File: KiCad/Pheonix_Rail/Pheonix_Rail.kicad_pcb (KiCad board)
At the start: 2 copper layers, 127 x 19.7 mm, 15 parts, among them J1 1729128, J10 1729128, J11 1729128, J12 1729128, J13 1729128, J2 1729128, J3 1729128, J4 1729128, J5 1729128, J6 1729128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

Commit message: commit
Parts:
- moved H2 170.9 mm to (267.2, 74.0)
- moved J1 90.0 mm to (144.3, 69.4)
- moved H1 62.9 mm to (145.8, 74.0)
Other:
- board size 127 x 19.7 mm -> 127 x 26 mm
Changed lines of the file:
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@@
 	)
 	(setup
+		(stackup
+			(layer "F.SilkS"
+				(type "Top Silk Screen")
+			)
+			(layer "F.Paste"
+				(type "Top Solder Paste")
+			)
+			(layer "F.Mask"
+				(type "Top Solder Mask")
+				(thickness 0.01)
+			)
+			(layer "F.Cu"
+				(type "copper")
+				(thickness 0.035)
+			)
+			(layer "dielectric 1"
+				(type "core")
+				(thickness 1.51)
+				(material "FR4")
+				(epsilon_r 4.5)
+				(loss_tangent 0.02)
+			)
+			(layer "B.Cu"
+				(type "copper")
+				(thickness 0.035)
+			)
+			(layer "B.Mask"
+				(type "Bottom Solder Mask")
+				(thickness 0.01)
+			)
+			(layer "B.Paste"
+				(type "Bottom Solder Paste")
+			)
+			(layer "B.SilkS"
+				(type "Bottom Silk Screen")
+			)
+			(copper_finish "None")
+			(dielectric_constraints no)
+		)
 		(pad_to_mask_clearance 0)
 		(allow_soldermask_bridges_in_footprints no)
@@
 	(footprint "MountingHole:MountingHole_2.5mm"
 		(layer "F.Cu")
-		(at 100.37 30.5)
+		(at 145.75 74)
 		(descr "Mounting Hole 2.5mm, no annular, generated by kicad-footprint-generator mountinghole.py")
 		(tags "mountinghole")
@@
 	(footprint "1729128:PHOENIX_1729128"
 		(layer "F.Cu")
-		(at 60.695 36.15)
+		(at 144.275 69.4)
 		(property "Reference" "J1"
 			(at 3.175 -9.135 0)
@@
 	(footprint "MountingHole:MountingHole_2.5mm"
 		(layer "F.Cu")
-		(at 100.37 37.05)
+		(at 267.25 74)
 		(descr "Mounting Hole 2.5mm, no annular, generated by kicad-footprint-generator mountinghole.py")
 		(tags "mountinghole")
@@
 	)
 	(gr_rect
-		(start 122.32 74.58)
-		(end 249.36 94.27)
+		(start 143 61)
+		(end 270 87)
 		(stroke
 			(width 0.05)

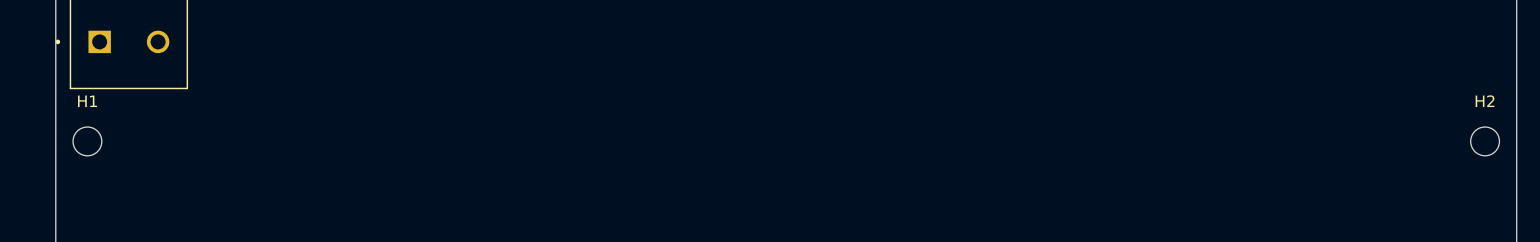
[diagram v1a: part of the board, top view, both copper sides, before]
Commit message: changed mounting holes
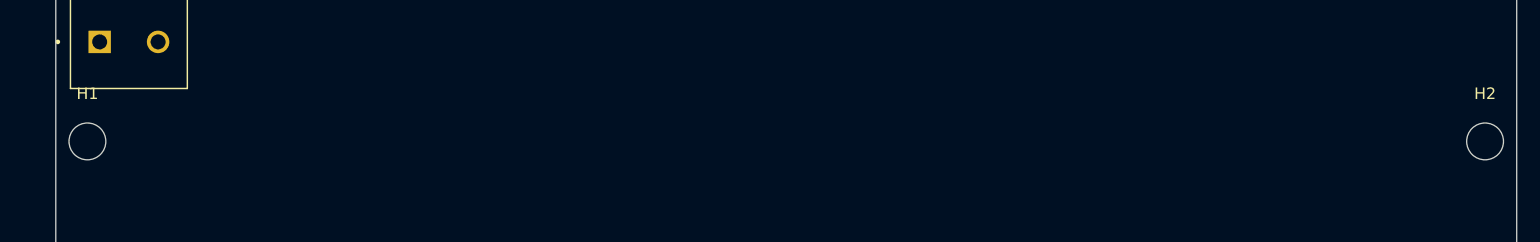
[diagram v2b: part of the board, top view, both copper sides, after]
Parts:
- H1, H2: footprint MountingHole:MountingHole_2.5mm -> MountingHole:MountingHole_3.2mm_M3
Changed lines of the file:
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@@
 		(embedded_fonts no)
 	)
-	(footprint "MountingHole:MountingHole_2.5mm"
+	(footprint "MountingHole:MountingHole_3.2mm_M3"
 		(layer "F.Cu")
 		(at 145.75 74)
-		(descr "Mounting Hole 2.5mm, no annular, generated by kicad-footprint-generator mountinghole.py")
-		(tags "mountinghole")
+		(descr "Mounting Hole 3.2mm, M3, no annular, generated by kicad-footprint-generator mountinghole.py")
+		(tags "mountinghole M3")
 		(property "Reference" "H1"
-			(at 0 -3.45 0)
+			(at 0 -4.15 0)
 			(layer "F.SilkS")
 			(effects
@@
 		)
 		(property "Value" "MountingHole"
-			(at 0 3.45 0)
+			(at 0 4.15 0)
 			(layer "F.Fab")
 			(effects
@@
 		(fp_circle
 			(center 0 0)
-			(end 2.5 0)
+			(end 3.2 0)
 			(stroke
 				(width 0.15)
@@
 		(fp_circle
 			(center 0 0)
-			(end 2.75 0)
+			(end 3.45 0)
 			(stroke
 				(width 0.05)
@@
 		(pad "" np_thru_hole circle
 			(at 0 0)
-			(size 2.5 2.5)
-			(drill 2.5)
+			(size 3.2 3.2)
+			(drill 3.2)
 			(layers "*.Cu" "*.Mask")
 		)
@@
 		(embedded_fonts no)
 	)
-	(footprint "MountingHole:MountingHole_2.5mm"
+	(footprint "MountingHole:MountingHole_3.2mm_M3"
 		(layer "F.Cu")
 		(at 267.25 74)
-		(descr "Mounting Hole 2.5mm, no annular, generated by kicad-footprint-generator mountinghole.py")
-		(tags "mountinghole")
+		(descr "Mounting Hole 3.2mm, M3, no annular, generated by kicad-footprint-generator mountinghole.py")
+		(tags "mountinghole M3")
 		(property "Reference" "H2"
-			(at 0 -3.45 0)
+			(at 0 -4.15 0)
 			(layer "F.SilkS")
 			(effects
@@
 		)
 		(property "Value" "MountingHole"
-			(at 0 3.45 0)
+			(at 0 4.15 0)
 			(layer "F.Fab")
 			(effects
@@
 		(fp_circle
 			(center 0 0)
-			(end 2.5 0)
+			(end 3.2 0)
 			(stroke
 				(width 0.15)
@@
 		(fp_circle
 			(center 0 0)
-			(end 2.75 0)
+			(end 3.45 0)
 			(stroke
 				(width 0.05)
@@
 		(pad "" np_thru_hole circle
 			(at 0 0)
-			(size 2.5 2.5)
-			(drill 2.5)
+			(size 3.2 3.2)
+			(drill 3.2)
 			(layers "*.Cu" "*.Mask")
 		)

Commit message: layout for phoenix board
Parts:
- moved J7 184.1 mm to (255.9, 70.0)
- moved J6 168.0 mm to (237.9, 70.0)
- moved J13 163.5 mm to (246.9, 85.0)
- moved J5 159.4 mm to (220.0, 70.0)
- moved J12 148.1 mm to (229.0, 85.0)
- moved J4 141.4 mm to (202.0, 70.0)
- moved J11 134.1 mm to (211.0, 85.0)
- moved J3 124.1 mm to (184.0, 70.0)
- moved J10 120.0 mm to (193.0, 85.0)
- moved J2 108.0 mm to (166.0, 70.0)
- moved J9 103.5 mm to (175.0, 85.0)
- moved J8 88.6 mm to (157.0, 85.0)
- moved J1 3.77 mm to (148.0, 70.0)
- moved H1 0.70 mm to (146.4, 74.0), turned to 180 degrees
- moved H2 0.70 mm to (266.6, 74.0), turned to 180 degrees
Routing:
- added copper zone on F.Cu, net +24V
- added copper zone on B.Cu, net GND
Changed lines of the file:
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@@
 	(footprint "1729128:PHOENIX_1729128"
 		(layer "F.Cu")
-		(at 73.43 36.15)
+		(at 237.9475 69.975)
 		(property "Reference" "J6"
-			(at 3.175 -9.135 0)
+			(at 4.5675 1.025 0)
 			(layer "F.SilkS")
 			(effects
@@
 	(footprint "1729128:PHOENIX_1729128"
 		(layer "F.Cu")
-		(at 73.43 45.85)
+		(at 255.9475 69.975)
 		(property "Reference" "J7"
-			(at 3.175 -9.135 0)
+			(at 4.5675 1.025 0)
 			(layer "F.SilkS")
 			(effects
@@
 	(footprint "1729128:PHOENIX_1729128"
 		(layer "F.Cu")
-		(at 73.43 55.55)
+		(at 157 85)
 		(property "Reference" "J8"
 			(at 3.175 -9.135 0)
@@
 	(footprint "1729128:PHOENIX_1729128"
 		(layer "F.Cu")
-		(at 86.165 36.15)
+		(at 211 85)
 		(property "Reference" "J11"
 			(at 3.175 -9.135 0)
@@
 	(footprint "1729128:PHOENIX_1729128"
 		(layer "F.Cu")
-		(at 60.695 55.55)
+		(at 184 70)
 		(property "Reference" "J3"
-			(at 3.175 -9.135 0)
+			(at 4.5675 1 0)
 			(layer "F.SilkS")
 			(effects
@@
 	(footprint "1729128:PHOENIX_1729128"
 		(layer "F.Cu")
-		(at 86.165 55.55)
+		(at 246.9475 84.975)
 		(property "Reference" "J13"
 			(at 3.175 -9.135 0)
@@
 	(footprint "1729128:PHOENIX_1729128"
 		(layer "F.Cu")
-		(at 86.165 45.85)
+		(at 229 85)
 		(property "Reference" "J12"
 			(at 3.175 -9.135 0)
@@
 	(footprint "MountingHole:MountingHole_3.2mm_M3"
 		(layer "F.Cu")
-		(at 145.75 74)
+		(at 146.45 74 180)
 		(descr "Mounting Hole 3.2mm, M3, no annular, generated by kicad-footprint-generator mountinghole.py")
 		(tags "mountinghole M3")
@@
 		)
 		(pad "" np_thru_hole circle
-			(at 0 0)
+			(at 0 0 180)
 			(size 3.2 3.2)
 			(drill 3.2)
@@
 	(footprint "1729128:PHOENIX_1729128"
 		(layer "F.Cu")
-		(at 60.695 74.95)
+		(at 220 70)
 		(property "Reference" "J5"
-			(at 3.175 -9.135 0)
+			(at 4.5675 1 0)
 			(layer "F.SilkS")
 			(effects
@@
 	(footprint "1729128:PHOENIX_1729128"
 		(layer "F.Cu")
-		(at 73.43 65.25)
+		(at 175 85)
 		(property "Reference" "J9"
 			(at 3.175 -9.135 0)
@@
 	(footprint "1729128:PHOENIX_1729128"
 		(layer "F.Cu")
-		(at 73.43 74.95)
+		(at 193 85)
 		(property "Reference" "J10"
 			(at 3.175 -9.135 0)
@@
 	(footprint "1729128:PHOENIX_1729128"
 		(layer "F.Cu")
-		(at 144.275 69.4)
+		(at 148 70)
 		(property "Reference" "J1"
-			(at 3.175 -9.135 0)
+			(at 5 1 0)
 			(layer "F.SilkS")
 			(effects
@@
 	(footprint "1729128:PHOENIX_1729128"
 		(layer "F.Cu")
-		(at 60.695 65.25)
+		(at 202 70)
 		(property "Reference" "J4"
-			(at 3.175 -9.135 0)
+			(at 4.5675 1 0)
 			(layer "F.SilkS")
 			(effects
@@
 	(footprint "1729128:PHOENIX_1729128"
 		(layer "F.Cu")
-		(at 60.695 45.85)
+		(at 166 70)
 		(property "Reference" "J2"
-			(at 3.175 -9.135 0)
+			(at 4.5675 1 0)
 			(layer "F.SilkS")
 			(effects
@@
 	(footprint "MountingHole:MountingHole_3.2mm_M3"
 		(layer "F.Cu")
-		(at 267.25 74)
+		(at 266.55 74 180)
 		(descr "Mounting Hole 3.2mm, M3, no annular, generated by kicad-footprint-generator mountinghole.py")
 		(tags "mountinghole M3")
@@
 		)
 		(pad "" np_thru_hole circle
-			(at 0 0)
+			(at 0 0 180)
 			(size 3.2 3.2)
 			(drill 3.2)
@@
 		)
 		(fill no)
+		(locked yes)
 		(layer "Edge.Cuts")
 	)
+	(zone
+		(net 1)
+		(net_name "+24V")
+		(layer "F.Cu")
+		(hatch edge 0.5)
+		(connect_pads
+			(clearance 0.5)
+		)
+		(min_thickness 0.25)
+		(filled_areas_thickness no)
+		(fill yes
+			(thermal_gap 0.5)
+			(thermal_bridge_width 0.5)
+		)
+		(polygon
+			(pts
+				(xy 142 60) (xy 271 60) (xy 271 88) (xy 142 88)
+			)
+		)
+	)
+	(zone
+		(net 2)
+		(net_name "GND")
+		(layer "B.Cu")
+		(hatch edge 0.5)
+		(priority 1)
+		(connect_pads
+			(clearance 0.5)
+		)
+		(min_thickness 0.25)
+		(filled_areas_thickness no)
+		(fill yes
+			(thermal_gap 0.5)
+			(thermal_bridge_width 0.5)
+		)
+		(polygon
+			(pts
+				(xy 142 60) (xy 271 60) (xy 271 88) (xy 142 88)
+			)
+		)
+	)
 	(embedded_fonts no)
